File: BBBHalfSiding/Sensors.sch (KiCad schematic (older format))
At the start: 27 parts, among them IC1 MCT6H, P1 In Track Out, P2 East (Points), P3 West Main (Frog, Normal), P4 ABS Slave Bus, P5 West Div. (Frog, Revesed), U10 74LV125AN, U7 TRS202E, U8 SN75LBC179, U9 TRS202E

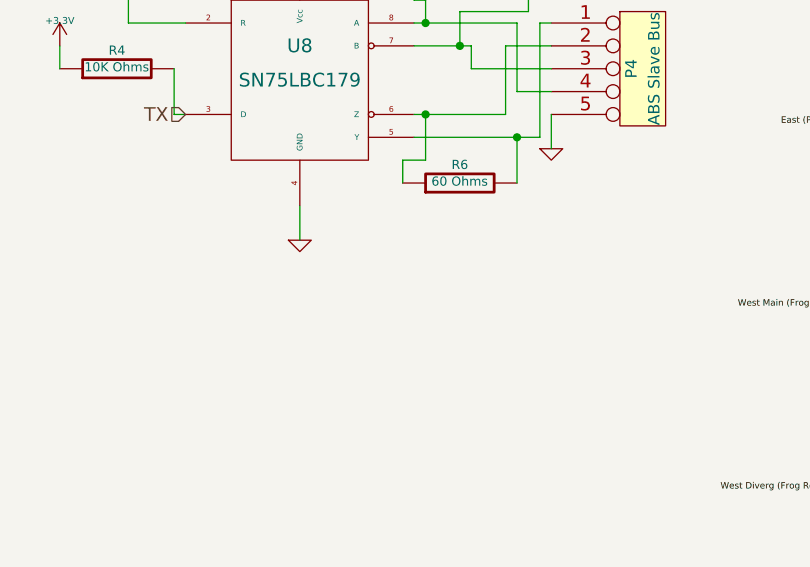
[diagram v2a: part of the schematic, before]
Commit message: Add missing bypass caps.
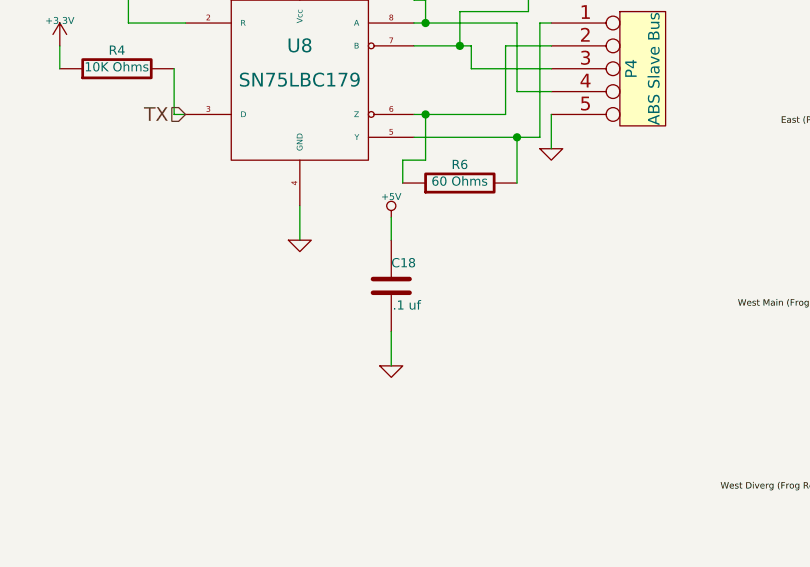
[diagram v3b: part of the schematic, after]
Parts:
- added C18: .1 uf, ~, symbol C
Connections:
- net +5V: now also C18.1
- net GND: now also C18.2
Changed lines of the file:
@@
 	0    1    1    0
 $EndComp
+$Comp
+L C C18
+U 1 1 5BCB53DC
+P 4950 5600
+F 0 "C18" H 4950 5700 40  0000 L CNN
+F 1 ".1 uf" H 4956 5515 40  0000 L CNN
+F 2 "~" H 4988 5450 30  0000 C CNN
+F 3 "~" H 4950 5600 60  0000 C CNN
+	1    4950 5600
+	1    0    0    -1
+$EndComp
+$Comp
+L +5V #PWR045
+U 1 1 5BCB53F7
+P 4950 5300
+F 0 "#PWR045" H 4950 5390 20  0001 C CNN
+F 1 "+5V" H 4950 5390 30  0000 C CNN
+F 2 "" H 4950 5300 60  0000 C CNN
+F 3 "" H 4950 5300 60  0000 C CNN
+	1    4950 5300
+	1    0    0    -1
+$EndComp
+$Comp
+L GND #PWR046
+U 1 1 5BCB5410
+P 4950 5950
+F 0 "#PWR046" H 4950 5950 30  0001 C CNN
+F 1 "GND" H 4950 5880 30  0001 C CNN
+F 2 "" H 4950 5950 60  0000 C CNN
+F 3 "" H 4950 5950 60  0000 C CNN
+	1    4950 5950
+	1    0    0    -1
+$EndComp
+Wire Wire Line
+	4950 5300 4950 5400
+Wire Wire Line
+	4950 5800 4950 5950
 $EndSCHEMATC
